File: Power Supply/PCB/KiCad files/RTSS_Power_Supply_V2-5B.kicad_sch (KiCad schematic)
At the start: 75 parts, among them J1 Barrel_Jack, J2 SMA_connector, J3 5V fan, J4 Conn_01x10_Pin, J5 12V fan, J6 Ext LED, J7 Conn_01x10_Socket, J8 Conn_01x01, Q1 IRFB4615, SW1 SW_SPST, U1 L7812, U2 ATtiny25-20S, U3 L7805, U4 OPA356xxDBV, U5 1EDN8511BXUSA1, Y1 8MHz

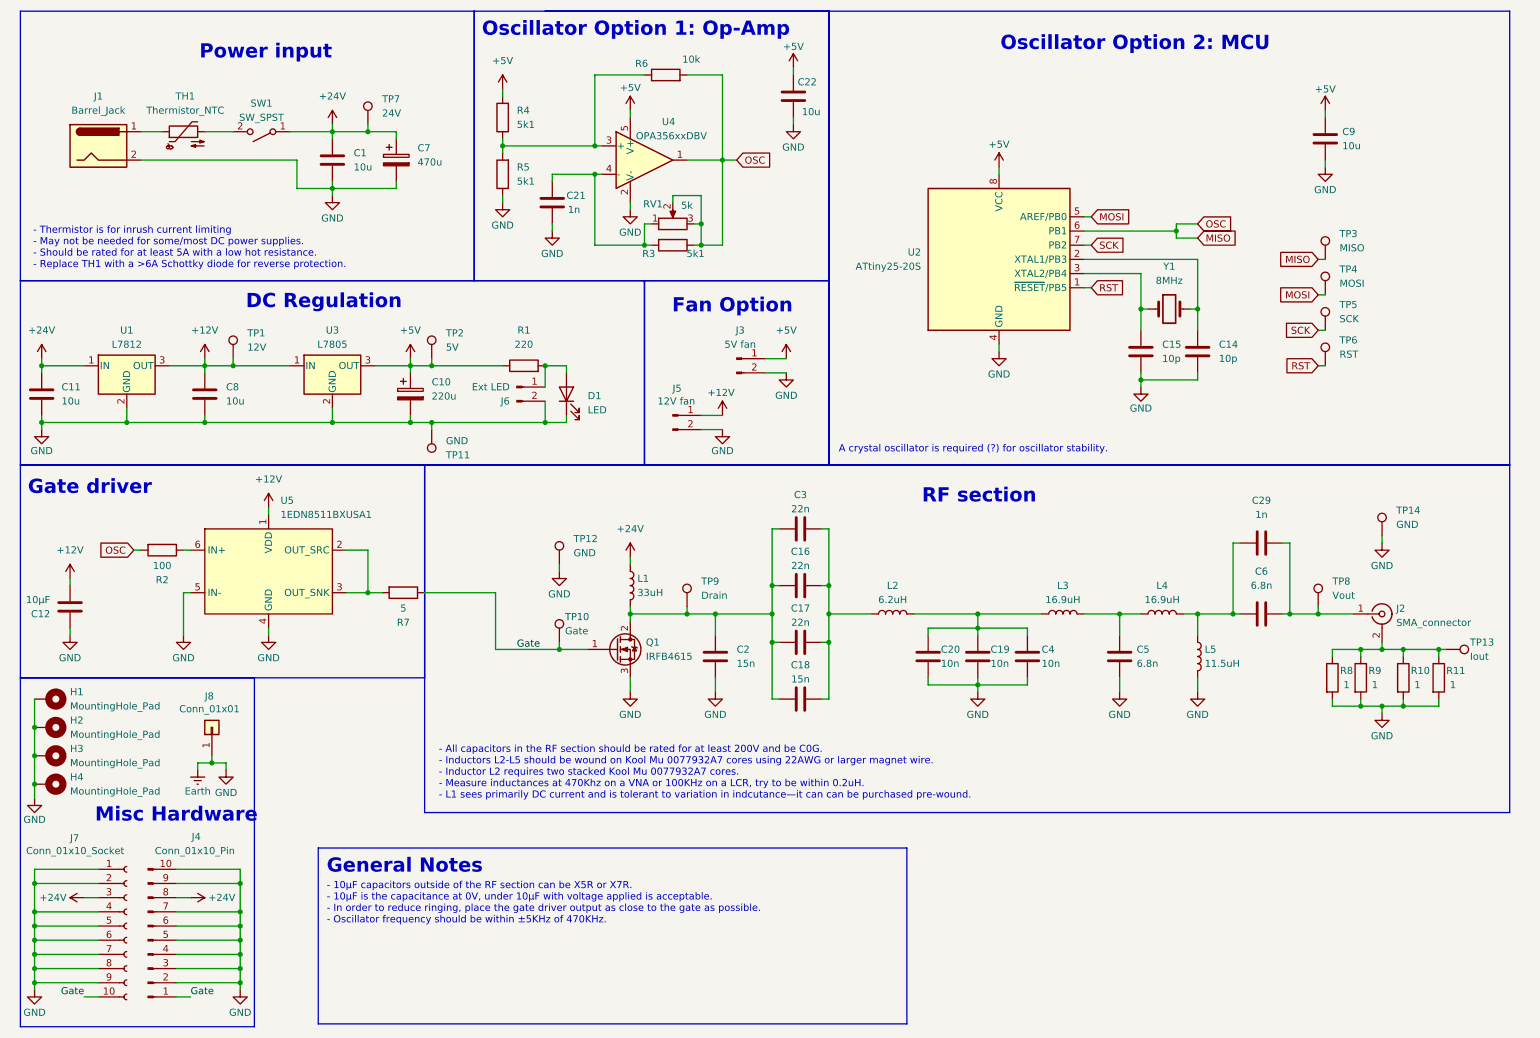
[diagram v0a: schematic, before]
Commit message: Release Power Supply V2.5B
In version 2.5B of the PCB, we have made a few improvements to reduce cost and increase reliability compared with version 2.3B1. Most notably the oscillator section has been redesigned to eliminate the need for a microcontroller and now only relies on a 7.6MHz crystal oscillator and TTL logic. To reduce costs, we have eliminated the daughterboard by moving everything onto the main board, additionally L2 has been updated to only use a single inductor core from the two cores required on previous versions. Moving all of this new hardware onto the main board has had the consequence of causing us to remove the TO-247 MOSFET option in favor of TO-220 to save space.
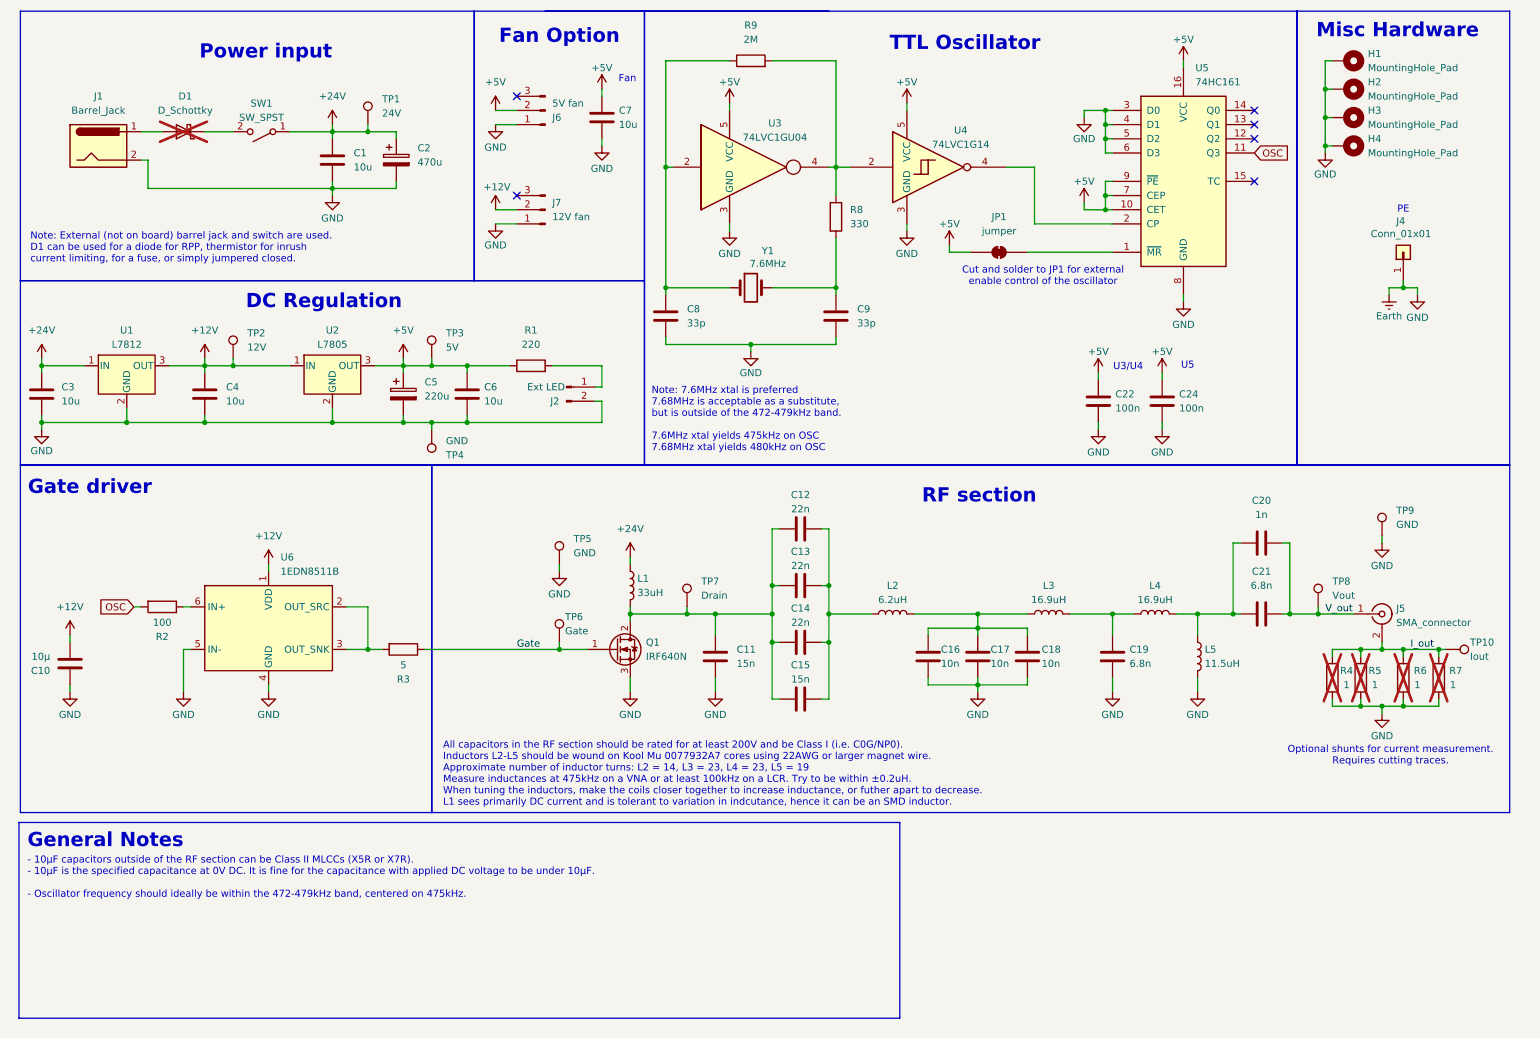
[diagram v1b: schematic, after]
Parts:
- removed C21: 1n, Capacitor_SMD:C_0805_2012Metric, symbol Device:C
- removed D1: LED, LED_SMD:LED_1206_3216Metric_Pad1.42x1.75mm_HandSolder, symbol Device:LED
- removed J3: 5V fan, Connector_PinHeader_2.54mm:PinHeader_1x02_P2.54mm_Vertical, symbol Connector:Conn_01x02_Pin
- removed J4: Conn_01x10_Pin, Connector_PinHeader_2.54mm:PinHeader_1x10_P2.54mm_Horizontal, symbol Connector:Conn_01x10_Pin
- removed J5: 12V fan, Connector_PinHeader_2.54mm:PinHeader_1x02_P2.54mm_Vertical, symbol Connector:Conn_01x02_Pin
- removed J7: Conn_01x10_Socket, Connector_PinSocket_2.54mm:PinSocket_1x10_P2.54mm_Vertical, symbol Connector:Conn_01x10_Socket
- removed J8: Conn_01x01, Connector_Wire:SolderWire-1sqmm_1x01_D1.4mm_OD2.7mm, symbol Connector_Generic:Conn_01x01
- removed R3: 5k, Resistor_SMD:R_0805_2012Metric, symbol Device:R
- removed R4, R5: 5k1, Resistor_SMD:R_0805_2012Metric, symbol Device:R
- removed R6: 10k, Resistor_SMD:R_0805_2012Metric, symbol Device:R
- removed RV1: 5k1, Potentiometer_SMD:Potentiometer_Bourns_TC33X_Vertical, symbol Device:R_Potentiometer
- removed TH1: Thermistor_NTC, Capacitor_THT:C_Disc_D11.0mm_W5.0mm_P5.00mm, symbol Device:Thermistor_NTC
- removed TP3: MISO, TestPoint:TestPoint_Pad_D1.0mm, symbol Connector:TestPoint
- removed TP4: MOSI, TestPoint:TestPoint_Pad_D1.0mm, symbol Connector:TestPoint
- removed TP5: SCK, TestPoint:TestPoint_Pad_D1.0mm, symbol Connector:TestPoint
- removed TP6: RST, TestPoint:TestPoint_Pad_D1.0mm, symbol Connector:TestPoint
- removed U2: ATtiny25-20S, Package_SO:SOIC-8_5.3x5.3mm_P1.27mm, symbol MCU_Microchip_ATtiny:ATtiny25-20S
- removed U4: OPA356xxDBV, Package_TO_SOT_SMD:SOT-23-5, symbol Amplifier_Operational:OPA356xxDBV
- added C24: 100n, Capacitor_SMD:C_0603_1608Metric, symbol Device:C
- added C6: 10u, Capacitor_SMD:C_1206_3216Metric_Pad1.33x1.80mm_HandSolder, symbol Device:C
- added D1: D_Schottky, Package_TO_SOT_THT:TO-220-2_Vertical, symbol Device:D_Schottky
- added J4: Conn_01x01, Connector_Wire:SolderWire-1sqmm_1x01_D1.4mm_OD2.7mm, symbol Connector_Generic:Conn_01x01
- added J6: 5V fan, Connector:FanPinHeader_1x03_P2.54mm_Vertical, symbol Connector:Conn_01x03_Pin
- added J7: 12V fan, Connector:FanPinHeader_1x03_P2.54mm_Vertical, symbol Connector:Conn_01x03_Pin
- added JP1: jumper, Jumper:SolderJumper-2_P1.3mm_Bridged_RoundedPad1.0x1.5mm, symbol Jumper:SolderJumper_2_Bridged
- added R8: 330, Resistor_SMD:R_0805_2012Metric, symbol Device:R
- added R9: 2M, Resistor_SMD:R_0805_2012Metric, symbol Device:R
- added U3: 74LVC1GU04, Package_TO_SOT_SMD:SOT-553, symbol 74xGxx:74LVC1GU04DRL
- added U4: 74LVC1G14, Package_TO_SOT_SMD:SOT-553, symbol 74xGxx:SN74LVC1G14DRL
- added U5: 74HC161, Package_SO:SOP-16_4.4x10.4mm_P1.27mm, symbol 74xx:74LS161
- C10: renamed from C12; value 10µF -> 10µ
- C11: renamed from C2; footprint Capacitor_SMD:C_1206_3216Metric_Pad1.33x1.80mm_HandSolder -> Capacitor_SMD:C_1210_3225Metric_Pad1.33x2.70mm_HandSolder
- C15: renamed from C18; footprint Capacitor_SMD:C_1206_3216Metric_Pad1.33x1.80mm_HandSolder -> Capacitor_SMD:C_1210_3225Metric_Pad1.33x2.70mm_HandSolder
- C19: renamed from C5; footprint Capacitor_SMD:C_1206_3216Metric_Pad1.33x1.80mm_HandSolder -> Capacitor_SMD:C_1210_3225Metric_Pad1.33x2.70mm_HandSolder
- C21: renamed from C6; footprint Capacitor_SMD:C_1206_3216Metric_Pad1.33x1.80mm_HandSolder -> Capacitor_SMD:C_1210_3225Metric_Pad1.33x2.70mm_HandSolder
- C22: value 10u -> 100n; footprint Capacitor_SMD:C_1206_3216Metric_Pad1.33x1.80mm_HandSolder -> Capacitor_SMD:C_0603_1608Metric
- C8: renamed from C15; value 10p -> 33p; footprint Capacitor_SMD:C_0805_2012Metric -> Capacitor_SMD:C_0603_1608Metric
- C9: renamed from C14; value 10p -> 33p; footprint Capacitor_SMD:C_0805_2012Metric -> Capacitor_SMD:C_0603_1608Metric
- J1, SW1: footprint Connector:JWT_A3963_1x02_P3.96mm_Vertical -> custom_parts:3D-JWT_A3963_1x02_P3.96mm_Vertical
- L2: footprint custom_parts:V2_L_Koolmu_2x_small_THT_0077932A7_1 -> custom_parts:L_Koolmu_1x_small_THTonly_0077932A7
- L3, L4, L5: footprint custom_parts:V2_L_Koolmu_1x_small_THT_0077932A7_1 -> custom_parts:L_Koolmu_1x_small_THTonly_0077932A7
- Q1: value IRFB4615 -> IRF640N; footprint custom_parts:TO-247_220_Vertical -> custom_parts:3D_TO-220-3_Vertical
- R1: footprint Resistor_SMD:R_1206_3216Metric_Pad1.30x1.75mm_HandSolder -> Capacitor_SMD:C_0805_2012Metric_Pad1.18x1.45mm_HandSolder
- R3: renamed from R7; footprint Resistor_SMD:R_0805_2012Metric -> custom_parts:Bridge_R_0805_2012Metric
- R4: renamed from R8; footprint Resistor_SMD:R_1206_3216Metric -> custom_parts:Bridge_R_1206_3216Metric; now not fitted; now left out of the parts list
- R5: renamed from R9; footprint Resistor_SMD:R_1206_3216Metric -> custom_parts:Bridge_R_1206_3216Metric; now not fitted; now left out of the parts list
- R6: renamed from R10; footprint Resistor_SMD:R_1206_3216Metric -> custom_parts:Bridge_R_1206_3216Metric; now not fitted; now left out of the parts list
- R7: renamed from R11; footprint Resistor_SMD:R_1206_3216Metric -> custom_parts:Bridge_R_1206_3216Metric; now not fitted; now left out of the parts list
- U6: renamed from U5; value 1EDN8511BXUSA1 -> 1EDN8511B
- Y1: value 8MHz -> 7.6MHz
- renumbered C3 to C12, C16 to C13, C17 to C14, C20 to C16, C19 to C17, C4 to C18, C7 to C2, C29 to C20, C11 to C3, C8 to C4, C10 to C5, C9 to C7, J6 to J2, J2 to J5, TP7 to TP1, TP13 to TP10, TP1 to TP2, TP2 to TP3, TP11 to TP4, TP12 to TP5, TP10 to TP6, TP9 to TP7, TP14 to TP9, U3 to U2
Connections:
- net +12V: now also J7.2 (Pin_2)
- net +5V: now also C24.1, C6.1, J6.2 (Pin_2), JP1.1 (A), U3.5 (VCC), U4.5 (VCC), U5.10 (CET), U5.16 (VCC), U5.7 (CEP), U5.9 (~{PE})
- net Earth: now also C24.2, C6.2, J4.1 (Pin_1), J6.1 (Pin_1), J7.1 (Pin_1), U3.3 (GND), U4.3 (GND), U5.3 (D0), U5.4 (D1), U5.5 (D2), U5.6 (D3), U5.8 (GND)
- net I_out: now reaches J5.2 (Ext), R4.1, R5.1, R6.1, R7.1, TP10.1
- net V_out: now reaches C20.2, C21.2, J5.1 (In), TP8.1
- net at C9.1, Y1.2: now also R8.2
- net at J1.1: now also D1.2 (A)
- net at C8.1, Y1.1: now also R9.1, U3.2
- net at SW1.2 (B): now also D1.1 (K)
- net MISO renamed OSC
- net OSC: now also U5.11 (Q3)
- new net: R8.1, R9.2, U3.4, U4.2
- new net: JP1.2 (B), U5.1 (~{MR})
- new net: U4.4, U5.2 (CP)
- no-connect marks 0 -> 6
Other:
- note added: "- 10µF capacitors outside of the RF section can be Class II MLCCs (X5R or X7R). - 10µF is the specified capacitance at 0V DC. It is fine for the capacitance with applied DC voltage to be under 10µF. - Oscillator frequency should ideally be within the 472-479kHz band, centered on 475kHz."
- note added: "All capacitors in the RF section should be rated for at least 200V and be Class I (i.e. C0G/NP0). Inductors L2-L5 should be wound on Kool Mu 0077932A7 cores using 22AWG or larger magnet wire. Approximate number of inductor turns: L2 = 14, L3 = 23, L4 = 23, L5 = 19 Measure inductances at 475kHz on a VNA or at least 100kHz on a LCR. Try to be within ±0.2uH. When tuning the inductors, make the coils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"
- note added: "Cut and solder to JP1 for external enable control of the oscillator"
- note added: "Fan"
- note added: "Note: 7.6MHz xtal is preferred 7.68MHz is acceptable as a substitute, but is outside of the 472-479kHz band. 7.6MHz xtal yields 475kHz on OSC 7.68MHz xtal yields 480kHz on OSC"
- note added: "Note: External (not on board) barrel jack and switch are used. D1 can be used for a diode for RPP, thermistor for inrush current limiting, for a fuse, or simply jumpered closed."
- note added: "Optional shunts for current measurement. Requires cutting traces."
- note added: "PE"
- note added: "TTL Oscillator"
- note added: "U3/U4"
- note added: "U5"
- note removed: "- 10µF capacitors outside of the RF section can be X5R or X7R. - 10µF is the capacitance at 0V, under 10µF with voltage applied is acceptable. - In order to reduce ringing, place the gate driver output as close to the gate as possible. - Oscillator frequency should be within ±5KHz of 470KHz."
- note removed: "- All capacitors in the RF section should be rated for at least 200V and be C0G. - Inductors L2-L5 should be wound on Kool Mu 0077932A7 cores using 22AWG or larger magnet wire. - Inductor L2 requires two stacked Kool Mu 0077932A7 cores. - Measure inductances at 470Khz on a VNA or 100KHz on a LCR, try to be within 0.2uH. - L1 sees primarily DC current and is tolerant to variation in indcutance—it 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"
- note removed: "- Thermistor is for inrush current limiting - May not be needed for some/most DC power supplies. - Should be rated for at least 5A with a low hot resistance. - Replace TH1 with a >6A Schottky diode for reverse protection."
- note removed: "A crystal oscillator is required (?) for oscillator stability."
- note removed: "Oscillator Option 1: Op-Amp"
- note removed: "Oscillator Option 2: MCU"
- title: RTSS 470KHz Power Supply -> RTSS 470kHz Power Supply
- moved on the sheet: C10, C19, C5, C7, C8, C9, J2, L3, L4, R1, R2, R3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
